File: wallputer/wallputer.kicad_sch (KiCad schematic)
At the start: 244 parts, among them J1 For ROM uploading and control, J2 DE9_Socket, J3 4x20 character display, Q1 BS250, Q2 2N7000, Q3 BS250, Q4 2N7000, Q5 BS170, Q6 BS170, Q7 BC547, SW1 Reset, SW2 step, SW3 switch clock, U1 W65C02SxP, U10 MAX232, U11 NE555P, U12 74HC04, U13 NE555P, U14 74HC14, U15 74HC93, U16 74HC04, U17 74HC04, U18 74HC04, U19 74HC04, U2 SST39SF010, U21 SST39SF010, U22 INND-TS40, U23 INND-TS40, U24 SST39SF010, U25 INND-TS40, U26 INND-TS40, U27 SST39SF010, U28 INND-TS40, U29 INND-TS40, U3 HM62256BLP, U32 NE555P, U4 74HC00, U5 74HC153, U6 W65C51NxP, U7 W65C22SxP, U8 74HC00, Y2 1.8432Mhz, Y3 1 MHz

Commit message: more components routed
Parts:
- removed D38, D39: D, Diode_THT:D_5KPW_P12.70mm_Horizontal, symbol Device:D
- removed unit 6 of U12
- removed unit 1 of U12
- added C15: 1000uF, Capacitor_THT:CP_Axial_L20.0mm_D10.0mm_P26.00mm_Horizontal, symbol Device:C_Polarized
- added C16, C17, C18, C19, C20, C21, C22, C23, C24, C25, C26, C27, C28, C29, C30, C31, C32, C33, C34, C35, C36, C37: 100nF, Capacitor_THT:C_Disc_D5.0mm_W2.5mm_P5.00mm, symbol Device:C
- added D2, D3: 1N4148, Diode_THT:D_DO-35_SOD27_P7.62mm_Horizontal, symbol Diode:1N4148
- added J4: Barrel_Jack, Connector_BarrelJack:BarrelJack_CUI_PJ-063AH_Horizontal, symbol Connector:Barrel_Jack
- added Q8: IRLZ44N, Package_TO_SOT_THT:TO-220-3_Vertical, symbol Transistor_FET:IRLZ44N
- added R124: 10k, Resistor_THT:R_Axial_DIN0204_L3.6mm_D1.6mm_P2.54mm_Vertical, symbol Device:R
- added R6: 100k, Resistor_THT:R_Axial_DIN0204_L3.6mm_D1.6mm_P2.54mm_Vertical, symbol Device:R
- added unit 1 of U18
- added unit 6 of U18
- added unit 1 of U4
- C12, C9: footprint Capacitor_THT:CP_Axial_L10.0mm_D4.5mm_P15.00mm_Horizontal -> Capacitor_THT:CP_Radial_D5.0mm_P2.00mm
- Q5, Q6: value BS170 -> IRLZ44N; footprint Package_TO_SOT_THT:TO-92_Inline -> Package_TO_SOT_THT:TO-220-3_Vertical; symbol Transistor_FET:BS170 -> Transistor_FET:IRLZ44N
- R100, R101, R102, R103, R104, R105, R106, R107, R108, R109, R110, R111, R112, R113, R114, R115, R116, R117, R118, R119, R120, R121, R122, R123, R15, R16, R17, R18, R19, R20, R21, R22, R23, R24, R25, R26, R51, R52, R55, R56, R57, R58, R59, R60, R61, R62, R63, R64, R68, R69, R70, R71, R72, R73, R74, R75, R76, R77, R78, R79, R80, R81, R82, R83, R84, R85, R86, R87, R88, R89, R90, R91, R92, R93, R94, R95, R96, R97, R98, R99: value 2.2k -> 1k
- SW2, SW3: footprint Button_Switch_THT:KSA_Tactile_SPST -> Button_Switch_THT:SW_PUSH_6mm_H4.3mm
- renumbered U18 to U12
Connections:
- net +5V: now also C15.1, C16.1, C17.1, C18.2, C19.1, C20.1, C21.1, C22.1, C23.1, C24.2, C25.1, C26.1, C27.1, C28.1, C29.1, C30.1, C31.1, C32.1, C33.1, C34.1, C35.1, C36.1, C37.1, J4.1, R124.2
- net A0: now also U12.3
- net A1: now also U12.11; no longer U12.5
- net A10: now also U17.1; no longer U16.11
- net A11: now also U17.13; no longer U16.13
- net A12: now also U17.3; no longer U17.1
- net A13: now also U17.11; no longer U17.5
- net A14: now also U17.5
- net A15: now also U17.9; no longer U17.3
- net A2: now also U12.5; no longer U12.3
- net A4: now also U16.1; no longer U12.11
- net A5: now also U16.13
- net A6: now also U16.3; no longer U16.1
- net A7: now also U16.11; no longer U16.5
- net A8: now also U16.5; no longer U16.3
- net A9: no longer U17.9
- net D0: now also U18.1; no longer J3.7 (Pin_7), R62.1, U17.11, U7.13 (PB3)
- net D1: now also U18.13; no longer J3.8 (Pin_8), R63.1, U17.13, U7.14 (PB4)
- net D2: now also U18.3; no longer J3.9 (Pin_9), R64.1, U18.1, U7.15 (PB5)
- net D3: now also U18.11; no longer J3.10 (Pin_10), R58.1, U18.5, U7.16 (PB6)
- net D4: now also U18.5; no longer U18.3
- net D6: now also U12.1; no longer U12.11
- net GND: now also U14.11, U14.13, U14.5, U14.9, U4.4, U4.5, C15.2, C16.2, C17.2, C18.1, C19.2, C20.2, C21.2, C22.2, C23.2, C24.1, C25.2, C26.2, C27.2, C28.2, C29.2, C30.2, C31.2, C32.2, C33.2, C34.2, C35.2, C36.2, C37.2, J4.2, Q8.2 (D), R6.1, U4.1, U4.2; no longer J3.1 (Pin_1), Q5.1 (D), Q6.1 (D)
- net IRQb: now also D2.2 (A), D3.2 (A)
- net SW_BUS_DEC: now also Q8.1 (G), R6.2
- net phi0: now also U5.7 (Qa); no longer U4.6
- net at D25.1 (K), D26.2 (A): now also U16.10; no longer U16.6
- net at D14.2 (A), D9.1 (K): now also U12.10; no longer U12.6
- net at Q2.3 (D), R101.1, R103.1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: now also R17.1, R68.1, R70.1, R71.1, R73.1, R75.1
- net at D21.1 (K), D22.2 (A): now also U16.12
- net at D15.1 (K), D16.2 (A): now also U12.6; no longer U12.4
- net at D43.1 (K), D44.2 (A): now also U17.6; no longer U17.4
- net at R23.1: now also J3.8 (Pin_8), U7.15 (PB5); no longer U7.6 (PA4)
- net at D47.1 (K), D48.2 (A): now also U18.2; no longer U17.10
- net at R52.1: now also U7.3 (PA1); no longer U7.18 (CB1)
- net at U6.26 (~{IRQ}): now also D2.1 (K)
- net at D41.1 (K), D42.2 (A): now also U17.10; no longer U17.6
- net at D23.1 (K), D24.2 (A): now also U16.4; no longer U16.2
- net at D55.1 (K), D56.2 (A): now also U18.6; no longer U18.4
- net at R20.1: now also U7.18 (CB1); no longer U7.3 (PA1)
- net at D28.1 (K), D30.2 (A): now also U16.6; no longer U16.4
- net at R4.1: now also Q6.1 (G); no longer Q6.2 (G)
- net at R51.1: now also U7.2 (PA0); no longer U7.19 (CB2)
- net at D51.1 (K), D52.2 (A): now also U18.4; no longer U18.2
- net at D37.1 (K), D40.2 (A): now also U17.4; no longer U17.2
- net at D19.1 (K), D20.2 (A): now also U16.2; no longer U12.10
- net at D59.1 (K), D60.2 (A): now also U12.2; no longer U12.10
- net at D53.1 (K), D54.2 (A): now also U18.10; no longer U18.6
- net at D1.1 (K), D5.2 (A): now also U12.4
- net at D49.1 (K), D50.2 (A): now also U18.12; no longer U17.12
- net at D33.1 (K), D34.2 (A): now also U17.2; no longer U16.10
- net at Q5.2 (D): now also Q6.2 (D), Q8.3 (S); no longer R5.2
- net at U1.38 (~{SO}): now also R124.1
- net at R26.1: now also J3.5 (Pin_5), U7.12 (PB2); no longer U7.9 (PA7)
- net at U7.40 (CA1): now also R60.1; no longer R55.1
- net at U7.21 (~{IRQ}): now also D3.1 (K)
- net at R57.1: now also U7.4 (PA2); no longer U7.17 (PB7)
- net at D35.1 (K), D36.2 (A): now also U17.12; no longer U16.12
- net at R19.1: now also U7.19 (CB2); no longer U7.2 (PA0)
- net at R22.1: now also J3.9 (Pin_9), U7.16 (PB6); no longer U7.5 (PA3)
- net at U15.12 (Q0), U15.2 (R0(1)), U5.14 (A): now also U15.1 (~{CKB})
- net at U7.39 (CA2): now also R59.1; no longer R56.1
- net at R21.1: now also J3.10 (Pin_10), U7.17 (PB7); no longer U7.4 (PA2)
- net at U7.7 (PA5): now also R63.1; no longer R24.1
- net at U7.8 (PA6): now also R62.1; no longer R25.1
- removed net EN: J3.5 (Pin_5), R60.1, U7.11 (PB1)
- removed net RS: J3.4 (Pin_4), R59.1, U7.10 (PB0)
- removed net R/W: J3.6 (Pin_6), R61.1, U7.12 (PB2)
- new net: Q5.1 (G), R5.2
- new net: J3.4 (Pin_4), R55.1, U7.11 (PB1)
- new net: R61.1, U7.9 (PA7)
- new net: J3.6 (Pin_6), R25.1, U7.13 (PB3)
- new net: J3.7 (Pin_7), R24.1, U7.14 (PB4)
- new net: R64.1, U7.6 (PA4)
- new net: R56.1, U7.10 (PB0)
- new net: R58.1, U7.5 (PA3)
- no-connect marks 63 -> 58
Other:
- note added: "Todo: - rp2040 board - pcb"
- note removed: "Todo: - missing symbols - switch logic for bus decoder - rp2040 board - pcb"
- moved on the sheet: BAR1, BAR2, C8, J3, R14, R19, R20, R21, R22, R23, R24, R25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

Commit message: finish 1st placing
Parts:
- added A1: RaspberryPi_Pico_W, Module:RaspberryPi_Pico_W_SMD_HandSolder, symbol MCU_Module:RaspberryPi_Pico_W
- added U20, U31, U35, U9: SN74LVC165A, Package_SO:TSSOP-16_4.4x5mm_P0.65mm, symbol Interface_Expansion:LTC4317
- added U30, U33, U34, U36: 74HCT595, Package_SO:TSSOP-16_4.4x5mm_P0.65mm, symbol 74xx:74HCT595
- J2: footprint Connector_Dsub:DSUB-9_Socket_EdgeMount_P2.77mm -> Connector_Dsub:DSUB-9_Pins_Horizontal_P2.77x2.84mm_EdgePinOffset4.94mm_Housed_MountingHolesOffset4.94mm
- RV1: footprint Potentiometer_THT:Potentiometer_ACP_CA6-H2,5_Horizontal -> Potentiometer_THT:Potentiometer_Alpha_RD901F-40-00D_Single_Vertical
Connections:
- net at R23.1, U7.15 (PB5): now also J3.6 (Pin_6); no longer J3.8 (Pin_8)
- net at R26.1, U7.12 (PB2): now also J3.9 (Pin_9); no longer J3.5 (Pin_5)
- net at R55.1, U7.11 (PB1): now also J3.10 (Pin_10); no longer J3.4 (Pin_4)
- net at R22.1, U7.16 (PB6): now also J3.5 (Pin_5); no longer J3.9 (Pin_9)
- net at R21.1, U7.17 (PB7): now also J3.4 (Pin_4); no longer J3.10 (Pin_10)
- net at R25.1, U7.13 (PB3): now also J3.8 (Pin_8); no longer J3.6 (Pin_6)
- new net: A1.13 (GND), A1.18 (GND), A1.23 (GND), A1.28 (GND), A1.3 (GND), A1.38 (GND), A1.8 (GND)
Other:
- note added: "TODO: design RP2040 board https://www.ti.com/lit/ds/symlink/sn74hct595.pdf?ts=1786272471170 https://www.ti.com/lit/ds/symlink/sn74lvc165a.pdf?ts=1786277088896&ref_url=https%253A%252F%252Fwww.ti.com%252Fproduct-category%252Flogic-voltage-translation%252Fflip-flops-latches-registers%252Fshift-registers%252Fproducts.html https://chatgpt.com/c/6a5e65af-5e64-83ed-a366-c72244979704"

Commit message: fix ERC and DRC problems
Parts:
- removed A1: RaspberryPi_Pico_W, Module:RaspberryPi_Pico_W_SMD_HandSolder, symbol MCU_Module:RaspberryPi_Pico_W
- removed U20, U31, U35, U9: SN74LVC165A, Package_SO:TSSOP-16_4.4x5mm_P0.65mm, symbol Interface_Expansion:LTC4317
- removed U30, U33, U34, U36: 74HCT595, Package_SO:TSSOP-16_4.4x5mm_P0.65mm, symbol 74xx:74HCT595
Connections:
- net GND: now also J3.1 (Pin_1)
- no-connect marks 58 -> 59
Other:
- note removed: "Todo: - rp2040 board - pcb"

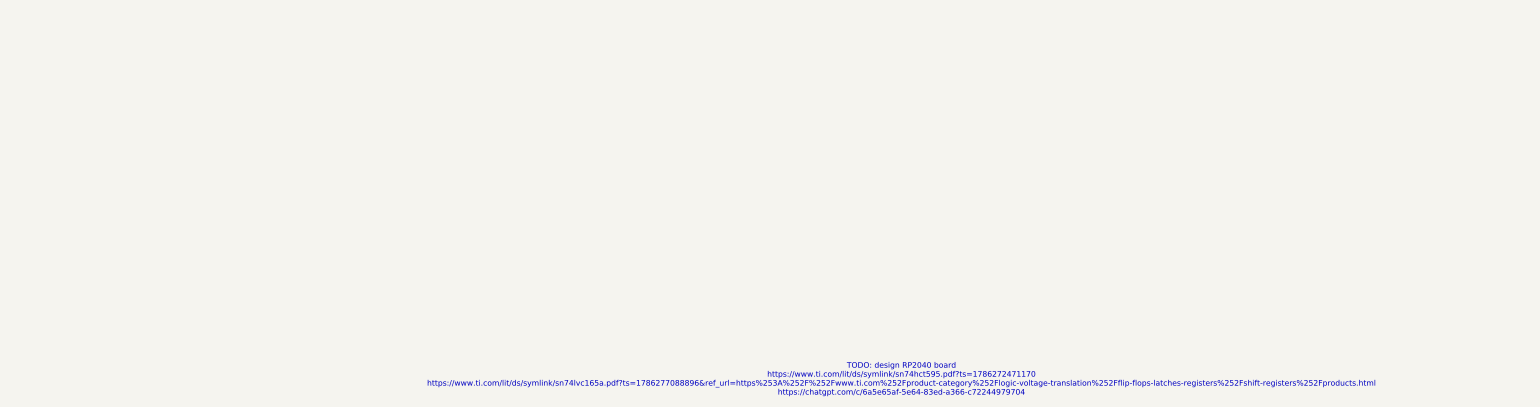
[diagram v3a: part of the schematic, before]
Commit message: ground plane + mounting holes
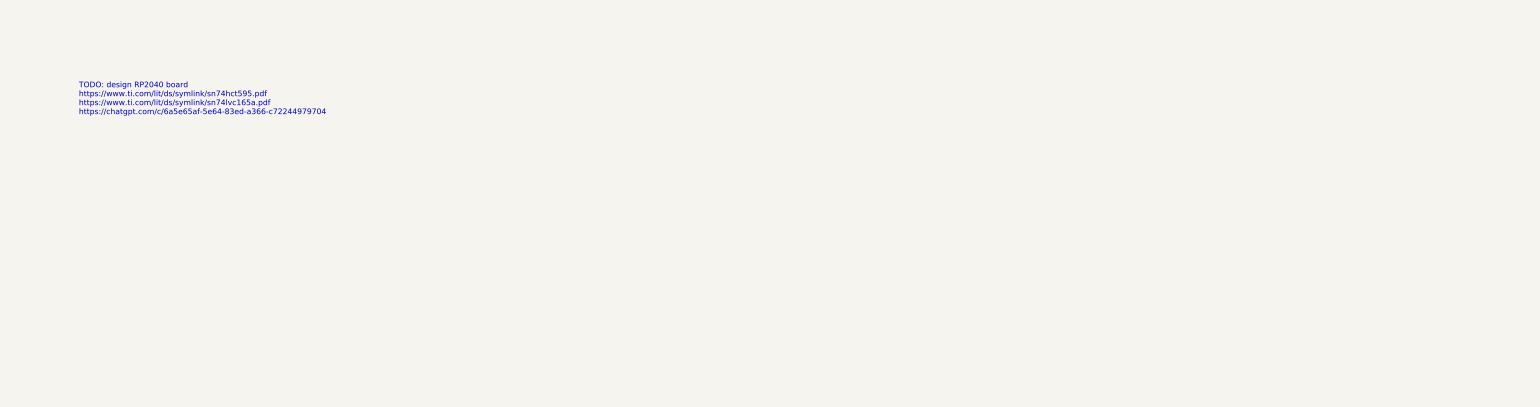
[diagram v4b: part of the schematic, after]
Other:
- note added: "TODO: design RP2040 board https://www.ti.com/lit/ds/symlink/sn74hct595.pdf https://www.ti.com/lit/ds/symlink/sn74lvc165a.pdf https://chatgpt.com/c/6a5e65af-5e64-83ed-a366-c72244979704"
- note removed: "TODO: design RP2040 board https://www.ti.com/lit/ds/symlink/sn74hct595.pdf?ts=1786272471170 https://www.ti.com/lit/ds/symlink/sn74lvc165a.pdf?ts=1786277088896&ref_url=https%253A%252F%252Fwww.ti.com%252Fproduct-category%252Flogic-voltage-translation%252Fflip-flops-latches-registers%252Fshift-registers%252Fproducts.html https://chatgpt.com/c/6a5e65af-5e64-83ed-a366-c72244979704"
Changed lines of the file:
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@@
 		)
 	)
-	(text "TODO: design RP2040 board\nhttps://www.ti.com/lit/ds/symlink/sn74hct595.pdf?ts=1786272471170\nhttps://www.ti.com/lit/ds/symlink/sn74lvc165a.pdf?ts=1786277088896&ref_url=https%253A%252F%252Fwww.ti.com%252Fproduct-category%252Flogic-voltage-translation%252Fflip-flops-latches-registers%252Fshift-registers%252Fproducts.html\nhttps://chatgpt.com/c/6a5e65af-5e64-83ed-a366-c72244979704"
+	(text "TODO: design RP2040 board\nhttps://www.ti.com/lit/ds/symlink/sn74hct595.pdf\nhttps://www.ti.com/lit/ds/symlink/sn74lvc165a.pdf\nhttps://chatgpt.com/c/6a5e65af-5e64-83ed-a366-c72244979704"
 		(exclude_from_sim no)
-		(at 673.354 446.786 0)
+		(at 485.648 382.778 0)
 		(effects
 			(font
 				(size 1.27 1.27)
 			)
+			(justify left)
 		)
 	)

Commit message: finish board
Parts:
- U22, U23, U25, U26, U28, U29: symbol New_Library:INND-TS40 -> New_Library:INND-TS40_1
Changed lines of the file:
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@@
 	(symbol
 		(lib_name "INND-TS40_1")
-		(lib_id "New_Library:INND-TS40")
+		(lib_id "New_Library:INND-TS40_1")
 		(at 158.75 187.96 0)
 		(unit 1)
@@
 	(symbol
 		(lib_name "INND-TS40_1")
-		(lib_id "New_Library:INND-TS40")
+		(lib_id "New_Library:INND-TS40_1")
 		(at 232.41 187.96 0)
 		(unit 1)
@@
 	(symbol
 		(lib_name "INND-TS40_1")
-		(lib_id "New_Library:INND-TS40")
+		(lib_id "New_Library:INND-TS40_1")
 		(at 85.09 187.96 0)
 		(unit 1)
@@
 	(symbol
 		(lib_name "INND-TS40_1")
-		(lib_id "New_Library:INND-TS40")
+		(lib_id "New_Library:INND-TS40_1")
 		(at 158.75 214.63 0)
 		(unit 1)
@@
 	(symbol
 		(lib_name "INND-TS40_1")
-		(lib_id "New_Library:INND-TS40")
+		(lib_id "New_Library:INND-TS40_1")
 		(at 232.41 214.63 0)
 		(unit 1)
@@
 	(symbol
 		(lib_name "INND-TS40_1")
-		(lib_id "New_Library:INND-TS40")
+		(lib_id "New_Library:INND-TS40_1")
 		(at 85.09 214.63 0)
 		(unit 1)
